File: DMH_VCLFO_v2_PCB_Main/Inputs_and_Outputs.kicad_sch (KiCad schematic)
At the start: 38 parts, among them J1 TS_Jack_6.35mm_Sw, J19 Conn_01x08, J2 TS_Jack_6.35mm_Sw, J200 IDC_02x05, J3 TS_Jack_6.35mm_Sw, J4 TS_Jack_6.35mm_Sw, J5 TS_Jack_6.35mm_Sw, J6 TS_Jack_6.35mm_Sw, J7 Conn_01x08, J8 Conn_01x08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

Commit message: Adjustments on breadboard
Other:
- note added: "U12B in BB"
- note added: "U12D in BB"
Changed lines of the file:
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@@
 		(comment 1 "PCB for 10cm Kosmo format synthesizer module")
+	)
+	(circle
+		(center 165.1 35.56)
+		(radius 3.81)
+		(stroke
+			(width 0)
+			(type default)
+		)
+		(fill
+			(type none)
+		)
+	)
+	(circle
+		(center 69.85 29.464)
+		(radius 3.81)
+		(stroke
+			(width 0)
+			(type default)
+		)
+		(fill
+			(type none)
+		)
+	)
+	(text "U12B in BB"
+		(exclude_from_sim no)
+		(at 165.1 30.226 0)
+		(effects
+			(font
+				(size 1.27 1.27)
+			)
+		)
+	)
+	(text "U12D in BB"
+		(exclude_from_sim no)
+		(at 69.85 24.13 0)
+		(effects
+			(font
+				(size 1.27 1.27)
+			)
+		)
 	)
 	(junction

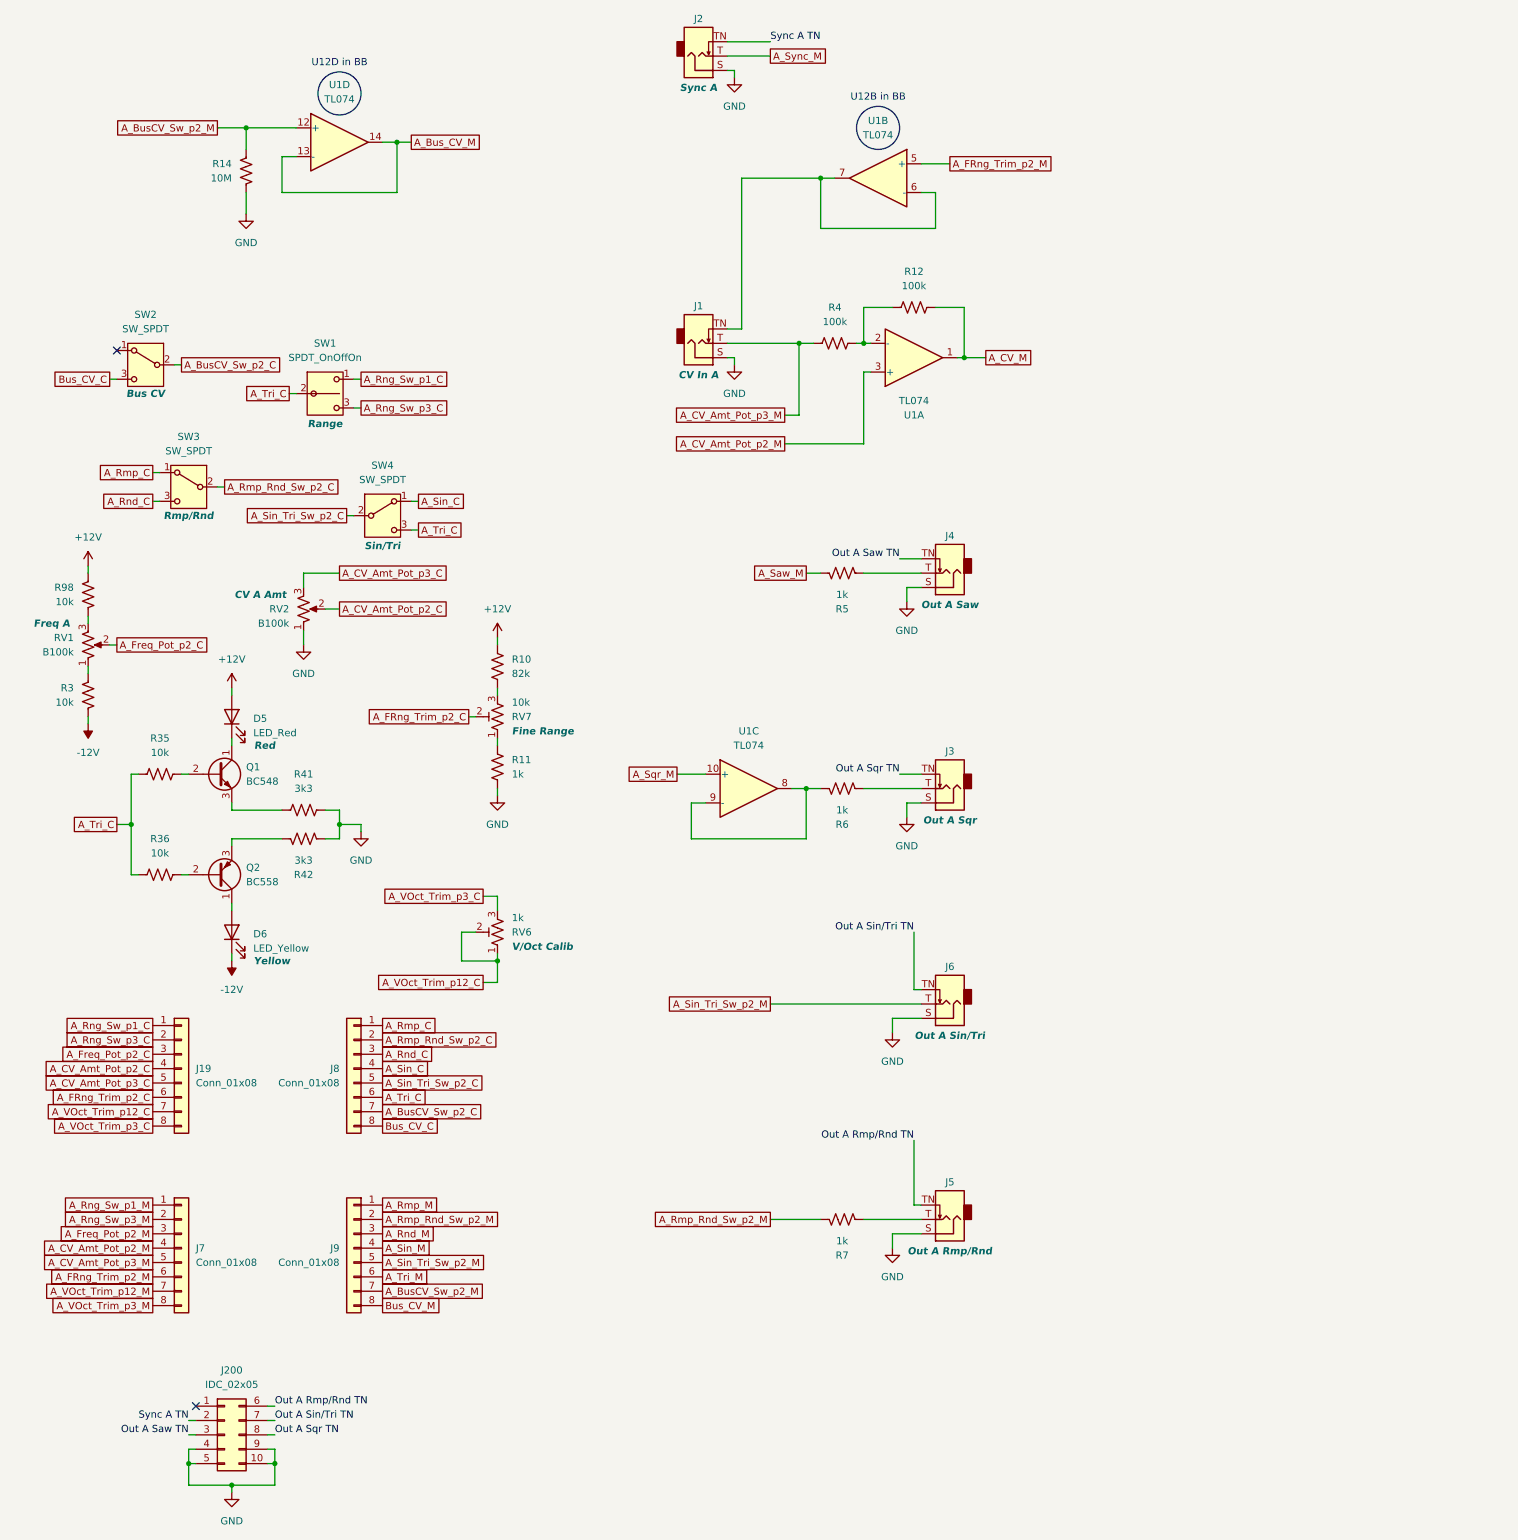
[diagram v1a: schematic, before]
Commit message: Rearranged IO page
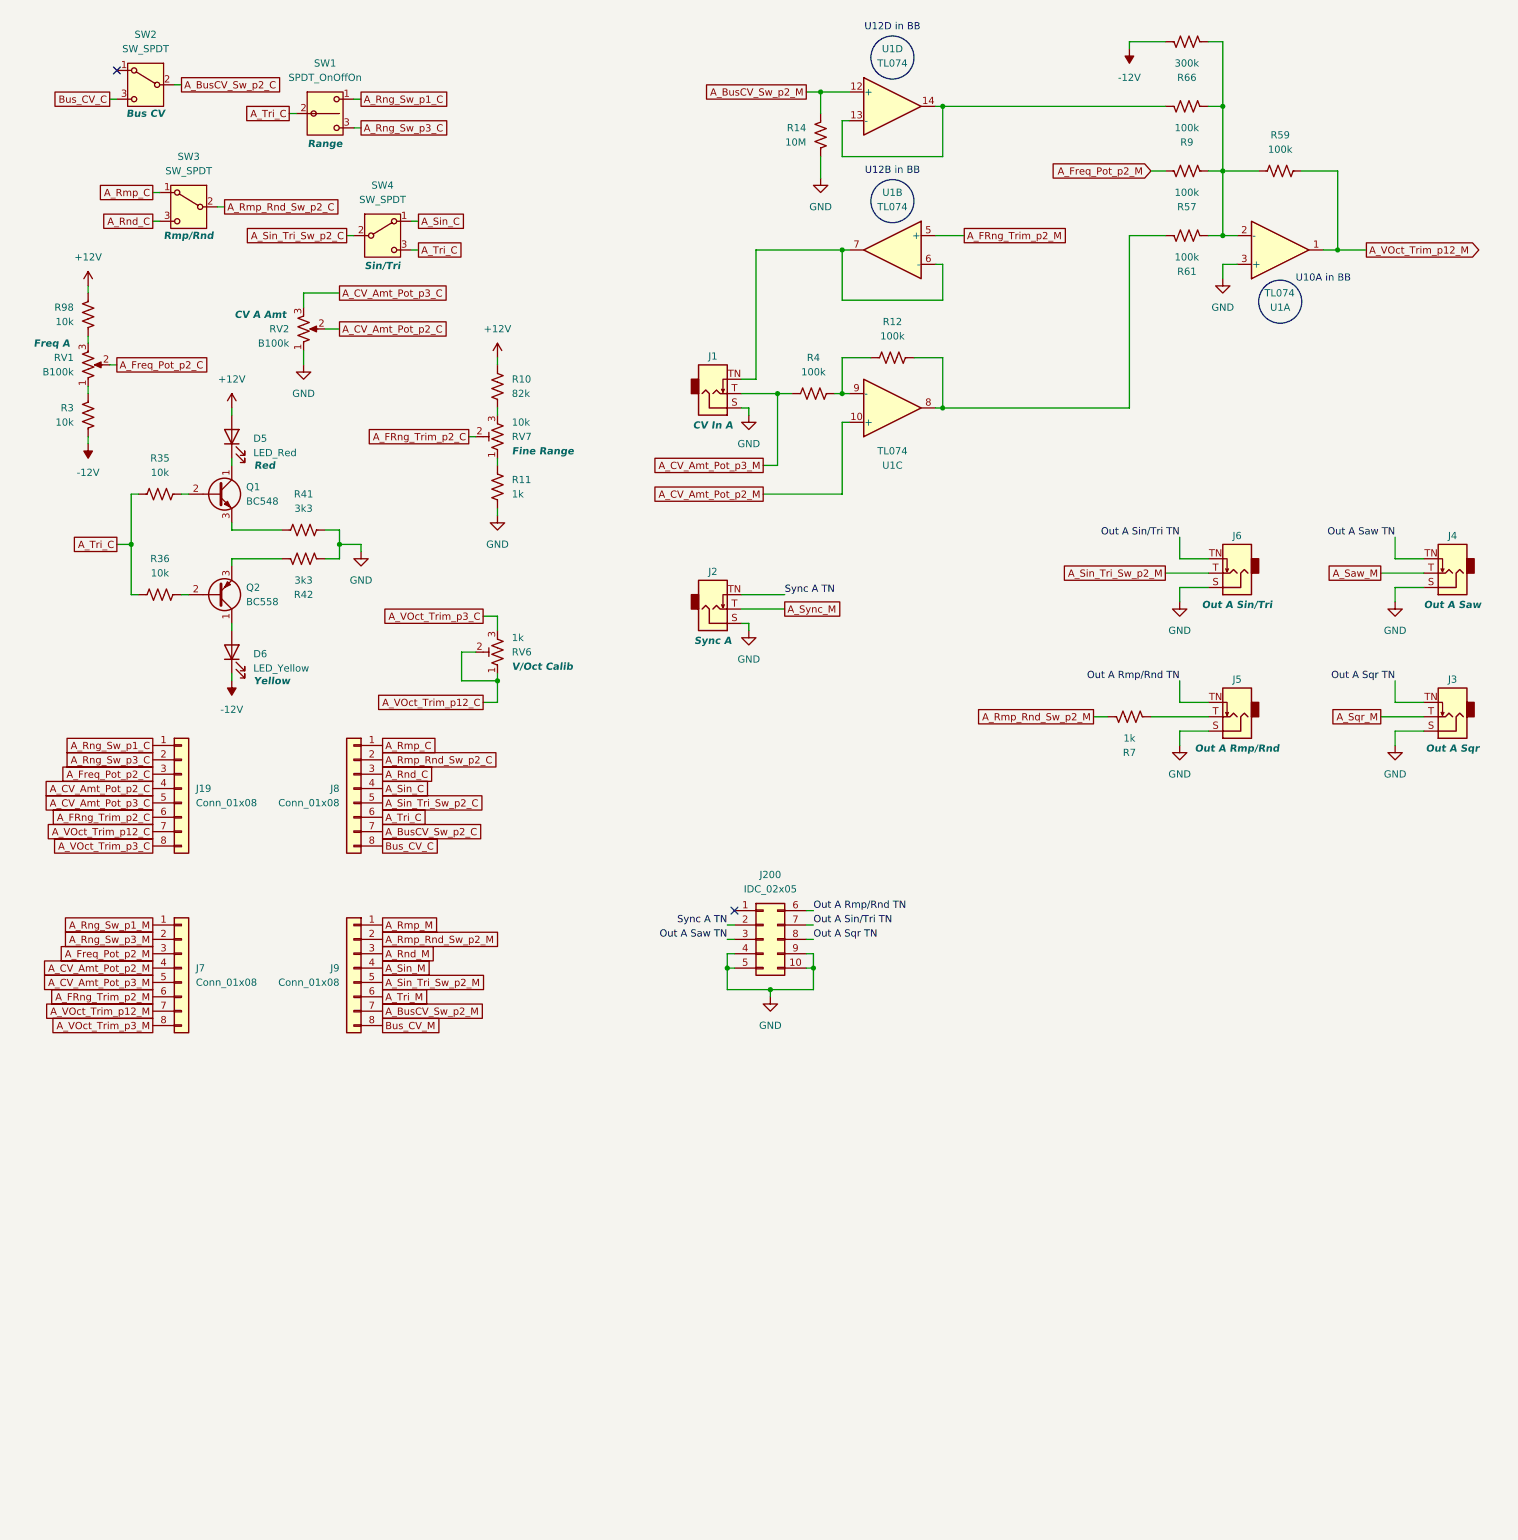
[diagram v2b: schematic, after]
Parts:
- removed R5, R6: 1k, Resistor_THT:R_Axial_DIN0207_L6.3mm_D2.5mm_P7.62mm_Horizontal, symbol Device:R_US
- removed unit 3 of U1
- added R57, R59, R61, R9: 100k, Resistor_THT:R_Axial_DIN0207_L6.3mm_D2.5mm_P7.62mm_Horizontal, symbol Device:R_US
- added R66: 300k, Resistor_THT:R_Axial_DIN0207_L6.3mm_D2.5mm_P7.62mm_Horizontal, symbol Device:R_US
- added unit 1 of U1
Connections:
- net -12V: now also R66.1
- net A_CV_Amt_Pot_p2_M: now also U1.10 (+); no longer U1.3 (+)
- net A_Freq_Pot_p2_M: now also R57.2
- net A_Saw_M: now also J4.T
- net A_Sqr_M: now also J3.T
- net A_VOct_Trim_p12_M: now also R59.2, U1.1
- net GND: now also U1.3 (+)
- net at R12.1, R4.2: now also U1.9 (-); no longer U1.2 (-)
- net A_Bus_CV_M: no longer names the net of U1.13 (-), U1.14
- net A_Bus_CV_M: now also R9.2
- net A_CV_M: no longer names the net of R12.2
- net A_CV_M: now also U1.8, R61.2; no longer U1.1
- new net: R57.1, R59.1, R61.1, R66.2, R9.1, U1.2 (-)
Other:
- note added: "U10A in BB"
- moved on the sheet: D5, D6, J1, J19, J2, J200, J3, J4, J5, J6, J7, J8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
